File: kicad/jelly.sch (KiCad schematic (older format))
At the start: 46 parts, among them M1 PAGER_MOTOR, M2 PAGER_MOTOR, P1 CONN_01X01, P10 CONN_01X01, P11 CONN_01X01, P12 CONN_01X01, P13 CONN_01X01, P14 CONN_01X01, P15 CONN_01X01, P2 CONN_01X01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

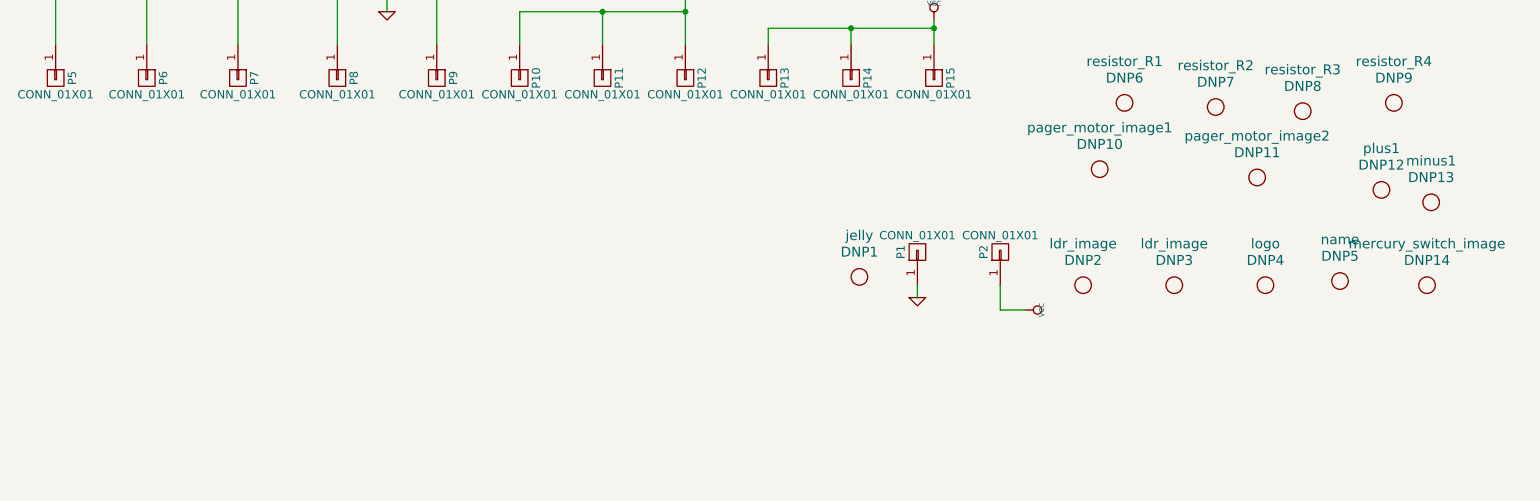
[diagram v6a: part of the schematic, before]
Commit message: Add creative commons logo
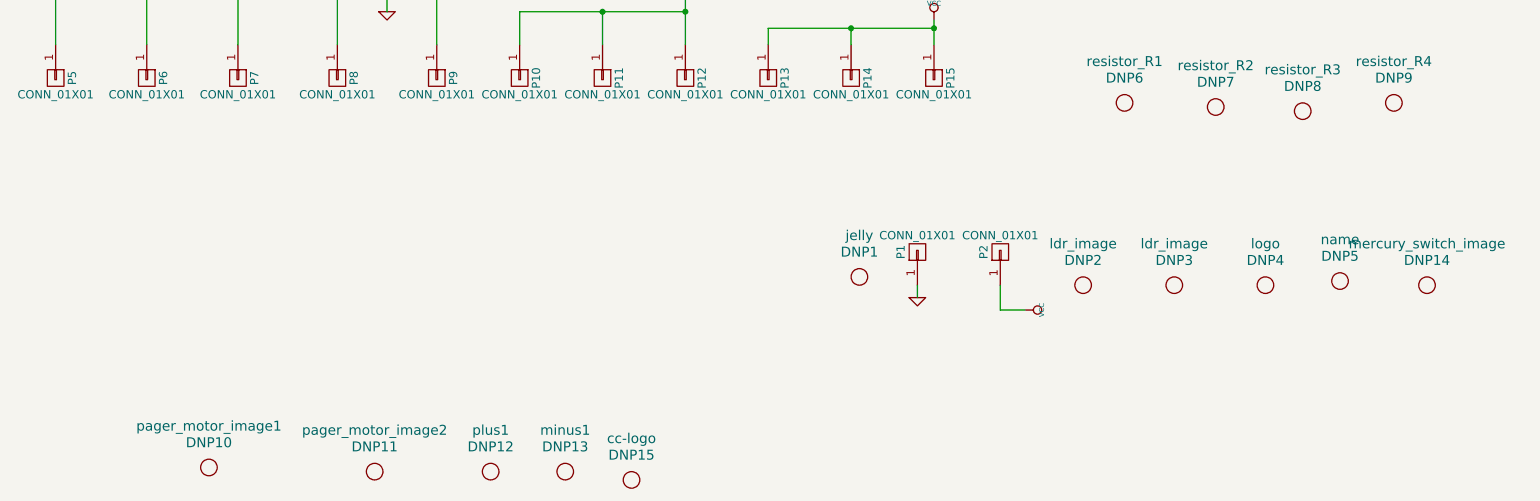
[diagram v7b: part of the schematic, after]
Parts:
- added DNP15: cc-logo, custom:cc_by_logo, symbol placeholder
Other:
- moved on the sheet: DNP10, DNP11, DNP12, DNP13
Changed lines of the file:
@@
 L placeholder DNP10
 U 1 1 5802A5F3
-P 8900 5500
-F 0 "DNP10" H 8900 5650 60  0000 C CNN
-F 1 "pager_motor_image1" H 8900 5750 60  0000 C CNN
-F 2 "custom:page_motor_image" H 8900 5650 60  0001 C CNN
-F 3 "" H 8900 5650 60  0001 C CNN
-	1    8900 5500
+P 3525 7300
+F 0 "DNP10" H 3525 7450 60  0000 C CNN
+F 1 "pager_motor_image1" H 3525 7550 60  0000 C CNN
+F 2 "custom:page_motor_image" H 3525 7450 60  0001 C CNN
+F 3 "" H 3525 7450 60  0001 C CNN
+	1    3525 7300
 	1    0    0    -1
 $EndComp
@@
 L placeholder DNP11
 U 1 1 5802A756
-P 9850 5550
-F 0 "DNP11" H 9850 5700 60  0000 C CNN
-F 1 "pager_motor_image2" H 9850 5800 60  0000 C CNN
-F 2 "custom:page_motor_image_flipped" H 9850 5700 60  0001 C CNN
-F 3 "" H 9850 5700 60  0001 C CNN
-	1    9850 5550
+P 4525 7325
+F 0 "DNP11" H 4525 7475 60  0000 C CNN
+F 1 "pager_motor_image2" H 4525 7575 60  0000 C CNN
+F 2 "custom:page_motor_image_flipped" H 4525 7475 60  0001 C CNN
+F 3 "" H 4525 7475 60  0001 C CNN
+	1    4525 7325
 	1    0    0    -1
 $EndComp
@@
 L placeholder DNP12
 U 1 1 5802B04C
-P 10600 5625
-F 0 "DNP12" H 10600 5775 60  0000 C CNN
-F 1 "plus1" H 10600 5875 60  0000 C CNN
-F 2 "custom:plus" H 10600 5775 60  0001 C CNN
-F 3 "" H 10600 5775 60  0001 C CNN
-	1    10600 5625
+P 5225 7325
+F 0 "DNP12" H 5225 7475 60  0000 C CNN
+F 1 "plus1" H 5225 7575 60  0000 C CNN
+F 2 "custom:plus" H 5225 7475 60  0001 C CNN
+F 3 "" H 5225 7475 60  0001 C CNN
+	1    5225 7325
 	1    0    0    -1
 $EndComp
@@
 L placeholder DNP13
 U 1 1 5802B75C
-P 10900 5700
-F 0 "DNP13" H 10900 5850 60  0000 C CNN
-F 1 "minus1" H 10900 5950 60  0000 C CNN
-F 2 "custom:minus" H 10900 5850 60  0001 C CNN
-F 3 "" H 10900 5850 60  0001 C CNN
-	1    10900 5700
+P 5675 7325
+F 0 "DNP13" H 5675 7475 60  0000 C CNN
+F 1 "minus1" H 5675 7575 60  0000 C CNN
+F 2 "custom:minus" H 5675 7475 60  0001 C CNN
+F 3 "" H 5675 7475 60  0001 C CNN
+	1    5675 7325
 	1    0    0    -1
 $EndComp
@@
 	1    0    0    -1
 $EndComp
+$Comp
+L placeholder DNP15
+U 1 1 5803B7B0
+P 6075 7375
+F 0 "DNP15" H 6075 7525 60  0000 C CNN
+F 1 "cc-logo" H 6075 7625 60  0000 C CNN
+F 2 "custom:cc_by_logo" H 6075 7525 60  0001 C CNN
+F 3 "" H 6075 7525 60  0001 C CNN
+	1    6075 7375
+	1    0    0    -1
+$EndComp

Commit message: Switch to stable kicad and re-plot
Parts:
- RV1, RV2: symbol POT -> POT-RESCUE-jelly
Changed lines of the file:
@@
 EESchema Schematic File Version 2
+LIBS:jelly-rescue
 LIBS:power
 LIBS:device
@@
 $EndComp
 $Comp
-L POT RV1
+L POT-RESCUE-jelly RV1
 U 1 1 57EC1656
 P 4950 3425
@@
 $EndComp
 $Comp
-L POT RV2
+L POT-RESCUE-jelly RV2
 U 1 1 57EC1E40
 P 8000 3400
